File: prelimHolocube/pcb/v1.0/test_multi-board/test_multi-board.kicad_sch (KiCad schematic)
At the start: 43 parts

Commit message: finish single board testing
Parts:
- removed R3: 10k, Resistor_THT:R_Axial_DIN0207_L6.3mm_D2.5mm_P7.62mm_Horizontal, symbol Device:R_US
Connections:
- net GND: now also U9.2 (GND)
- net RES: now also U9.11 (D35)
- net +12V renamed +13.5V
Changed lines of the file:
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@@
 	(wire
 		(pts
+			(xy 245.11 63.5) (xy 252.73 63.5)
+		)
+		(stroke
+			(width 0)
+			(type default)
+		)
+	)
+	(wire
+		(pts
 			(xy 158.75 193.04) (xy 115.57 193.04)
 		)
@@
 	(global_label "RES"
 		(shape input)
-		(at 252.73 73.66 0)
+		(at 252.73 63.5 0)
 		(fields_autoplaced yes)
 		(effects
@@
 		)
 		(property "Intersheetrefs" "${INTERSHEET_REFS}"
-			(at 259.3437 73.66 0)
+			(at 259.3437 63.5 0)
 			(effects
 				(font
@@
 			)
 		)
-		(property "Value" "+12V"
+		(property "Value" "+13.5V"
 			(at 102.87 43.18 90)
 			(effects
@@
 			)
 		)
-		(property "Value" "+12V"
+		(property "Value" "+13.5V"
 			(at 102.87 179.07 90)
 			(effects
@@
 	)
 	(symbol
+		(lib_id "power:GND")
+		(at 245.11 40.64 90)
+		(unit 1)
+		(exclude_from_sim no)
+		(in_bom yes)
+		(on_board yes)
+		(dnp no)
+		(property "Reference" "#PWR045"
+			(at 251.46 40.64 0)
+			(effects
+				(font
+					(size 1.27 1.27)
+				)
+				(hide yes)
+			)
+		)
+		(property "Value" "GND"
+			(at 250.444 40.64 90)
+			(effects
+				(font
+					(size 1.27 1.27)
+				)
+			)
+		)
+		(property "Footprint" ""
+			(at 245.11 40.64 0)
+			(effects
+				(font
+					(size 1.27 1.27)
+				)
+				(hide yes)
+			)
+		)
+		(property "Datasheet" ""
+			(at 245.11 40.64 0)
+			(effects
+				(font
+					(size 1.27 1.27)
+				)
+				(hide yes)
+			)
+		)
+		(property "Description" "Power symbol creates a global label with name \"GND\" , ground"
+			(at 245.11 40.64 0)
+			(effects
+				(font
+					(size 1.27 1.27)
+				)
+				(hide yes)
+			)
+		)
+		(pin "1"
+		)
+		(instances
+			(project "test_multi-board"
+				(path "/364c5bf3-0078-465d-b9ac-45c99f916d6d"
+					(reference "#PWR045")
+					(unit 1)
+				)
+			)
+		)
+	)
+	(symbol
 		(lib_id "Device:C_US")
 		(at 106.68 185.42 0)
@@
 			)
 		)
-		(property "Value" "+12V"
+		(property "Value" "+13.5V"
 			(at 29.21 134.62 90)
 			(effects
@@
 			)
 		)
-		(property "Value" "+12V"
+		(property "Value" "+13.5V"
 			(at 102.87 134.62 90)
 			(effects
@@
 	(symbol
 		(lib_id "Device:R_US")
-		(at 248.92 73.66 90)
-		(unit 1)
-		(exclude_from_sim no)
-		(in_bom yes)
-		(on_board yes)
-		(dnp no)
-		(property "Reference" "R3"
-			(at 246.38 76.454 90)
-			(effects
-				(font
-					(size 1.27 1.27)
-				)
-			)
-		)
-		(property "Value" "10k"
-			(at 251.46 76.454 90)
-			(effects
-				(font
-					(size 1.27 1.27)
-				)
-			)
-		)
-		(property "Footprint" "Resistor_THT:R_Axial_DIN0207_L6.3mm_D2.5mm_P7.62mm_Horizontal"
-			(at 249.174 72.644 90)
-			(effects
-				(font
-					(size 1.27 1.27)
-				)
-				(hide yes)
-			)
-		)
-		(property "Datasheet" "~"
-			(at 248.92 73.66 0)
-			(effects
-				(font
-					(size 1.27 1.27)
-				)
-				(hide yes)
-			)
-		)
-		(property "Description" "Resistor, US symbol"
-			(at 248.92 73.66 0)
-			(effects
-				(font
-					(size 1.27 1.27)
-				)
-				(hide yes)
-			)
-		)
-		(pin "1"
-		)
-		(pin "2"
-		)
-		(instances
-			(project ""
-				(path "/364c5bf3-0078-465d-b9ac-45c99f916d6d"
-					(reference "R3")
-					(unit 1)
-				)
-			)
-		)
-	)
-	(symbol
-		(lib_id "Device:R_US")
 		(at 152.4 186.69 90)
 		(unit 1)
@@
 			)
 		)
-		(property "Value" "+12V"
+		(property "Value" "+13.5V"
 			(at 29.21 179.07 90)
 			(effects
@@
 			)
 		)
-		(property "Value" "+12V"
+		(property "Value" "+13.5V"
 			(at 29.21 43.18 90)
 			(effects
@@
 			)
 		)
-		(property "Value" "+12V"
+		(property "Value" "+13.5V"
 			(at 102.87 88.9 90)
 			(effects
@@
 			)
 		)
-		(property "Value" "+12V"
+		(property "Value" "+13.5V"
 			(at 226.06 132.0799 90)
 			(effects
@@
 			)
 		)
-		(property "Value" "+12V"
+		(property "Value" "+13.5V"
 			(at 29.21 88.9 90)
 			(effects

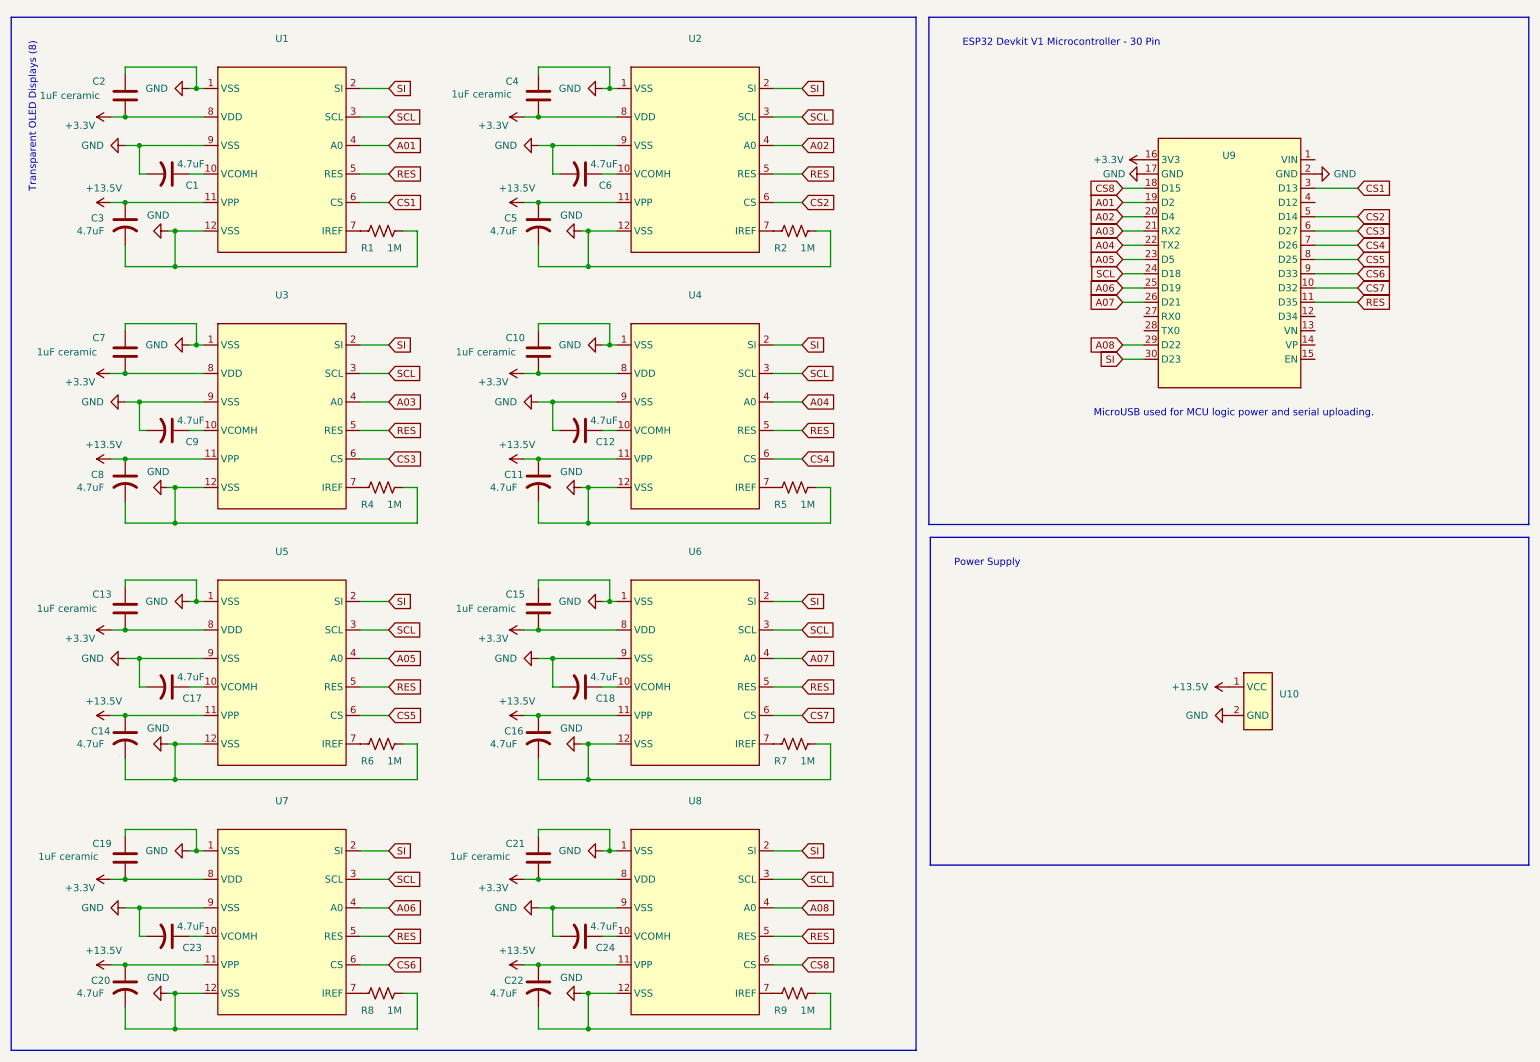
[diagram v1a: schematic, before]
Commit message: Finish schematic
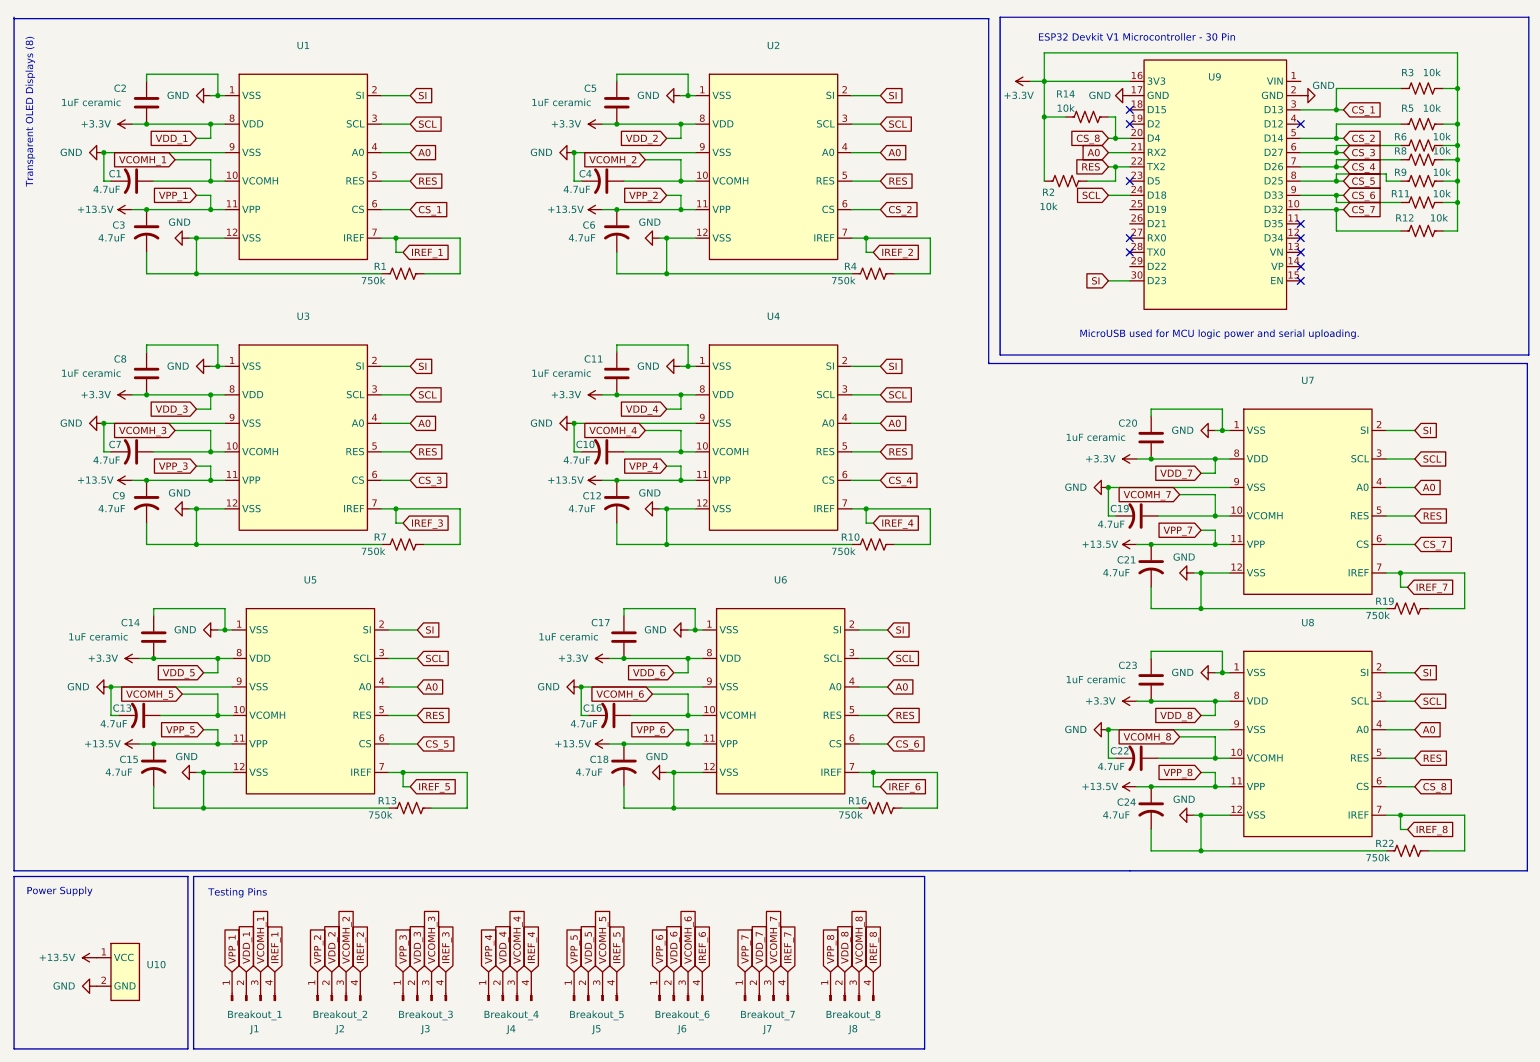
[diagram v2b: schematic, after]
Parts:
- removed C10, C13, C15, C19, C21, C4, C7: 1uF ceramic, Capacitor_THT:CP_Radial_D5.0mm_P2.50mm, symbol Device:C
- removed C11, C14, C17, C20, C23, C5, C8: 4.7uF, Capacitor_THT:CP_Radial_D4.0mm_P2.00mm, symbol Device:C_US
- added C10, C13, C15, C19, C21, C4, C7: 4.7uF, Capacitor_THT:CP_Radial_D4.0mm_P2.00mm, symbol Device:C_US
- added C11, C14, C17, C20, C23, C5, C8: 1uF ceramic, Capacitor_THT:CP_Radial_D5.0mm_P2.50mm, symbol Device:C
- added J1: Breakout_1, symbol Connector:Conn_01x04_Pin
- added J2: Breakout_2, symbol Connector:Conn_01x04_Pin
- added J3: Breakout_3, symbol Connector:Conn_01x04_Pin
- added J4: Breakout_4, symbol Connector:Conn_01x04_Pin
- added J5: Breakout_5, symbol Connector:Conn_01x04_Pin
- added J6: Breakout_6, symbol Connector:Conn_01x04_Pin
- added J7: Breakout_7, symbol Connector:Conn_01x04_Pin
- added J8: Breakout_8, symbol Connector:Conn_01x04_Pin
- added R10, R13, R16, R19, R22: 750k, Resistor_THT:R_Axial_DIN0207_L6.3mm_D2.5mm_P7.62mm_Horizontal, symbol Device:R_US
- added R11, R12, R14, R3: 10k, symbol Device:R_US
- R1, R4, R7: value 1M -> 750k
- R2, R5, R6, R8, R9: value 1M -> 10k; footprint Resistor_THT:R_Axial_DIN0207_L6.3mm_D2.5mm_P7.62mm_Horizontal -> (none)
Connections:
- net A03 is gone; now on net A0: U3.4 (A0), U9.21 (RX2)
- net CS2 is gone; now on net CS_2: U2.6 (CS), U9.5 (D14)
- net CS3 is gone; now on net CS_3: U3.6 (CS), U9.6 (D27)
- net CS4 is gone; now on net CS_4: U4.6 (CS), U9.7 (D26)
- net CS5 is gone; now on net CS_5: U5.6 (CS), U9.8 (D25)
- net +13.5V: now also C12.1, C18.1, C24.1, C6.1, C9.1, C15.1, C21.1, J1.1 (Pin_1), J2.1 (Pin_1), J3.1 (Pin_1), J4.1 (Pin_1), J5.1 (Pin_1), J6.1 (Pin_1), J7.1 (Pin_1), J8.1 (Pin_1); no longer C16.1, C22.1
- net +3.3V: now also R2.2, R5.2, R6.2, R8.2, R9.2, C11.2, C14.2, C17.2, C20.2, C23.2, C5.2, C8.2, J1.2 (Pin_2), J2.2 (Pin_2), J3.2 (Pin_2), J4.2 (Pin_2), J5.2 (Pin_2), J6.2 (Pin_2), J7.2 (Pin_2), J8.2 (Pin_2), R11.2, R12.2, R14.2, R3.2
- net GND: now also R1.1, R4.1, R7.1, C10.2, C11.1, C13.2, C14.1, C15.2, C17.1, C19.2, C20.1, C21.2, C23.1, C4.2, C5.1, C7.2, C8.1, R10.1, R13.1, R16.1, R19.1, R22.1; no longer R1.2, R2.2, R4.2, R5.2, R6.2, R7.2, R8.2, R9.2
- net RES: now also R2.1, U9.22 (TX2); no longer U9.11 (D35)
- net VCOMH_8: now reaches U8.10 (VCOMH)
- net VCOMH_8: now also C22.1, J8.3 (Pin_3); no longer C24.1
- net CS_5: now reaches R9.1
- net CS_5: no longer U8.7 (IREF)
- net VCOMH_3: now reaches U3.10 (VCOMH)
- net VCOMH_3: now also C7.1, J3.3 (Pin_3); no longer C9.1
- net VCOMH_7: now reaches U7.10 (VCOMH)
- net VCOMH_7: now also C19.1, J7.3 (Pin_3)
- net CS_3: now reaches R6.1
- net CS_3: no longer U5.7 (IREF)
- net IREF_1: now reaches U1.7 (IREF)
- net IREF_1: now also R1.2, J1.4 (Pin_4); no longer R1.1
- net CS_4: now reaches R8.1
- net CS_4: no longer U7.7 (IREF)
- net VCOMH_5: now reaches U5.10 (VCOMH)
- net VCOMH_5: now also C13.1, J5.3 (Pin_3)
- net VCOMH_1: now reaches C1.1, U1.10 (VCOMH)
- net VCOMH_1: now also J1.3 (Pin_3)
- net VCOMH_6: now reaches U6.10 (VCOMH)
- net VCOMH_6: now also C16.1, J6.3 (Pin_3); no longer C18.1
- net IREF_6: now reaches U6.7 (IREF)
- net IREF_6: now also J6.4 (Pin_4), R16.2; no longer R7.1
- net IREF_2: now reaches U2.7 (IREF)
- net IREF_2: now also R4.2, J2.4 (Pin_4); no longer R2.1
- net VCOMH_4: now reaches U4.10 (VCOMH)
- net VCOMH_4: now also C10.1, J4.3 (Pin_3); no longer C12.1
- net VCOMH_2: now reaches U2.10 (VCOMH)
- net VCOMH_2: now also C4.1, J2.3 (Pin_3); no longer C6.1
- net IREF_3: now reaches U3.7 (IREF)
- net IREF_3: now also R7.2, J3.4 (Pin_4); no longer R4.1
- net CS_2: now reaches R5.1
- net CS_2: no longer U4.7 (IREF)
- net A01: no longer names the net of U9.19 (D2)
- net A01: no longer U1.4 (A0)
- net A02 renamed A0
- net A0: now also U1.4 (A0), U4.4 (A0), U5.4 (A0), U6.4 (A0), U7.4 (A0), U8.4 (A0); no longer U9.20 (D4)
- removed net A04: U4.4 (A0), U9.22 (TX2)
- net A05: no longer names the net of U9.23 (D5)
- net A05: no longer U5.4 (A0)
- net A06: no longer names the net of U9.25 (D19)
- net A06: no longer U7.4 (A0)
- net A07: no longer names the net of U9.26 (D21)
- net A07: no longer U6.4 (A0)
- net A08: no longer names the net of U9.29 (D22)
- net A08: no longer U8.4 (A0)
- net CS1 renamed CS_1
- net CS_1: now also R3.1
- net CS6 renamed CS_6
- net CS_6: now also U6.6 (CS), R11.1; no longer U7.6 (CS)
- net CS7 renamed CS_7
- net CS_7: now also U7.6 (CS), R12.1; no longer U6.6 (CS)
- net CS8: no longer names the net of U9.18 (D15)
- net CS8: no longer U8.6 (CS)
- new net CS_8: R14.1, U8.6 (CS), U9.20 (D4)
- new net IREF_4: J4.4 (Pin_4), R10.2, U4.7 (IREF)
- new net IREF_5: J5.4 (Pin_4), R13.2, U5.7 (IREF)
- new net IREF_7: J7.4 (Pin_4), R19.2, U7.7 (IREF)
- new net IREF_8: J8.4 (Pin_4), R22.2, U8.7 (IREF)
- no-connect marks 0 -> 11
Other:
- note added: "Testing Pins"
- moved on the sheet: C1, C2, C3, R1, U1, U10, U9

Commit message: assign footprints multiboard pt 1
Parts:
- C11, C14, C17, C2, C20, C23, C5, C8: footprint Capacitor_THT:CP_Radial_D5.0mm_P2.50mm -> Capacitor_THT:C_Disc_D6.0mm_W2.5mm_P5.00mm
- J1, J2, J3, J4, J5, J6, J7, J8: footprint (none) -> Connector_PinHeader_2.54mm:PinHeader_1x04_P2.54mm_Vertical
- R11, R12, R14, R2, R3, R5, R6, R8, R9: footprint (none) -> Resistor_THT:R_Axial_DIN0207_L6.3mm_D2.5mm_P7.62mm_Horizontal
- U10: footprint Power_Supply:DC_2-Terminals -> Connector_PinHeader_2.54mm:PinHeader_1x02_P2.54mm_Vertical
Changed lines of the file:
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@@
 			)
 		)
-		(property "Footprint" "Capacitor_THT:CP_Radial_D5.0mm_P2.50mm"
+		(property "Footprint" "Capacitor_THT:C_Disc_D6.0mm_W2.5mm_P5.00mm"
 			(at 216.8652 134.62 0)
 			(effects
@@
 			)
 		)
-		(property "Footprint" ""
+		(property "Footprint" "Connector_PinHeader_2.54mm:PinHeader_1x04_P2.54mm_Vertical"
 			(at 161.29 187.96 0)
 			(effects
@@
 			)
 		)
-		(property "Footprint" ""
+		(property "Footprint" "Resistor_THT:R_Axial_DIN0207_L6.3mm_D2.5mm_P7.62mm_Horizontal"
 			(at 264.414 30.734 90)
 			(effects
@@
 			)
 		)
-		(property "Footprint" ""
+		(property "Footprint" "Resistor_THT:R_Axial_DIN0207_L6.3mm_D2.5mm_P7.62mm_Horizontal"
 			(at 264.414 34.544 90)
 			(effects
@@
 			)
 		)
-		(property "Footprint" "Capacitor_THT:CP_Radial_D5.0mm_P2.50mm"
+		(property "Footprint" "Capacitor_THT:C_Disc_D6.0mm_W2.5mm_P5.00mm"
 			(at 37.7952 80.01 0)
 			(effects
@@
 			)
 		)
-		(property "Footprint" ""
+		(property "Footprint" "Resistor_THT:R_Axial_DIN0207_L6.3mm_D2.5mm_P7.62mm_Horizontal"
 			(at 200.406 42.926 90)
 			(effects
@@
 			)
 		)
-		(property "Footprint" "Capacitor_THT:CP_Radial_D5.0mm_P2.50mm"
+		(property "Footprint" "Capacitor_THT:C_Disc_D6.0mm_W2.5mm_P5.00mm"
 			(at 216.8652 91.44 0)
 			(effects
@@
 			)
 		)
-		(property "Footprint" "Power_Supply:DC_2-Terminals"
+		(property "Footprint" "Connector_PinHeader_2.54mm:PinHeader_1x02_P2.54mm_Vertical"
 			(at 33.02 182.88 0)
 			(effects
@@
 			)
 		)
-		(property "Footprint" ""
+		(property "Footprint" "Connector_PinHeader_2.54mm:PinHeader_1x04_P2.54mm_Vertical"
 			(at 85.09 187.96 0)
 			(effects
@@
 			)
 		)
-		(property "Footprint" ""
+		(property "Footprint" "Connector_PinHeader_2.54mm:PinHeader_1x04_P2.54mm_Vertical"
 			(at 100.33 187.96 0)
 			(effects
@@
 			)
 		)
-		(property "Footprint" "Capacitor_THT:CP_Radial_D5.0mm_P2.50mm"
+		(property "Footprint" "Capacitor_THT:C_Disc_D6.0mm_W2.5mm_P5.00mm"
 			(at 37.7952 31.75 0)
 			(effects
@@
 			)
 		)
-		(property "Footprint" ""
+		(property "Footprint" "Resistor_THT:R_Axial_DIN0207_L6.3mm_D2.5mm_P7.62mm_Horizontal"
 			(at 264.414 40.894 90)
 			(effects
@@
 			)
 		)
-		(property "Footprint" ""
+		(property "Footprint" "Connector_PinHeader_2.54mm:PinHeader_1x04_P2.54mm_Vertical"
 			(at 130.81 187.96 0)
 			(effects
@@
 			)
 		)
-		(property "Footprint" ""
+		(property "Footprint" "Resistor_THT:R_Axial_DIN0207_L6.3mm_D2.5mm_P7.62mm_Horizontal"
 			(at 264.414 49.784 90)
 			(effects
@@
 			)
 		)
-		(property "Footprint" ""
+		(property "Footprint" "Connector_PinHeader_2.54mm:PinHeader_1x04_P2.54mm_Vertical"
 			(at 146.05 187.96 0)
 			(effects
@@
 			)
 		)
-		(property "Footprint" "Capacitor_THT:CP_Radial_D5.0mm_P2.50mm"
+		(property "Footprint" "Capacitor_THT:C_Disc_D6.0mm_W2.5mm_P5.00mm"
 			(at 122.8852 127 0)
 			(effects
@@
 			)
 		)
-		(property "Footprint" ""
+		(property "Footprint" "Resistor_THT:R_Axial_DIN0207_L6.3mm_D2.5mm_P7.62mm_Horizontal"
 			(at 264.414 37.084 90)
 			(effects
@@
 			)
 		)
-		(property "Footprint" "Capacitor_THT:CP_Radial_D5.0mm_P2.50mm"
+		(property "Footprint" "Capacitor_THT:C_Disc_D6.0mm_W2.5mm_P5.00mm"
 			(at 121.6152 31.75 0)
 			(effects
@@
 			)
 		)
-		(property "Footprint" ""
+		(property "Footprint" "Connector_PinHeader_2.54mm:PinHeader_1x04_P2.54mm_Vertical"
 			(at 54.61 187.96 0)
 			(effects
@@
 			)
 		)
-		(property "Footprint" ""
+		(property "Footprint" "Connector_PinHeader_2.54mm:PinHeader_1x04_P2.54mm_Vertical"
 			(at 69.85 187.96 0)
 			(effects
@@
 			)
 		)
-		(property "Footprint" "Capacitor_THT:CP_Radial_D5.0mm_P2.50mm"
+		(property "Footprint" "Capacitor_THT:C_Disc_D6.0mm_W2.5mm_P5.00mm"
 			(at 39.0652 127 0)
 			(effects
@@
 			)
 		)
-		(property "Footprint" "Capacitor_THT:CP_Radial_D5.0mm_P2.50mm"
+		(property "Footprint" "Capacitor_THT:C_Disc_D6.0mm_W2.5mm_P5.00mm"
 			(at 121.6152 80.01 0)
 			(effects
@@
 			)
 		)
-		(property "Footprint" ""
+		(property "Footprint" "Resistor_THT:R_Axial_DIN0207_L6.3mm_D2.5mm_P7.62mm_Horizontal"
 			(at 264.414 44.704 90)
 			(effects
@@
 			)
 		)
-		(property "Footprint" ""
+		(property "Footprint" "Connector_PinHeader_2.54mm:PinHeader_1x04_P2.54mm_Vertical"
 			(at 115.57 187.96 0)
 			(effects
@@
 			)
 		)
-		(property "Footprint" ""
+		(property "Footprint" "Resistor_THT:R_Axial_DIN0207_L6.3mm_D2.5mm_P7.62mm_Horizontal"
 			(at 264.414 24.384 90)
 			(effects
@@
 			)
 		)
-		(property "Footprint" ""
+		(property "Footprint" "Resistor_THT:R_Axial_DIN0207_L6.3mm_D2.5mm_P7.62mm_Horizontal"
 			(at 204.216 31.496 90)
 			(effects
